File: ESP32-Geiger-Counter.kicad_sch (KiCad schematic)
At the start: 85 parts, among them J1 2s1p Lipo Battery Pack (8.4V-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, J2 USB_C_Receptacle_USB2.0_16P, J5 Conn_01x07, Q1 STN1HNK60, Q3 2N7002, Q4 AO3401A, Q5 MMBT3904, SW1 SW_SPDT, SW2 RESET, SW3 BOOT, U1 BQ25886RGE, U2 AP63203WU, U3 ESP32-S3-WROOM-1, U4 UCC27517DBVR, U5 USBLC6-2SC6, U6 SBM-20 Geiger Mueller Tube

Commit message: layout changes
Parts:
- SW1: footprint Button_Switch_THT:SW_Slide_SPDT_Straight_CK_OS102011MS2Q -> Button_Switch_THT:SW_Slide_SPDT_Angled_CK_OS102011MA1Q
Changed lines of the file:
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@@
 			)
 		)
-		(property "Footprint" "Button_Switch_THT:SW_Slide_SPDT_Straight_CK_OS102011MS2Q"
+		(property "Footprint" "Button_Switch_THT:SW_Slide_SPDT_Angled_CK_OS102011MA1Q"
 			(at 153.67 46.99 0)
 			(hide yes)

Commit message: added test points
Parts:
- added TP_3.3V1: 3.3V, TestPoint:TestPoint_Keystone_5015_Micro_Mini, symbol Connector:TestPoint
- added TP_GND1: GND, TestPoint:TestPoint_Keystone_5015_Micro_Mini, symbol Connector:TestPoint
- added TP_HV_SENSE1: HV_SENSE, TestPoint:TestPoint_Keystone_5015_Micro_Mini, symbol Connector:TestPoint
- added TP_PULSE1: PULSE, TestPoint:TestPoint_Keystone_5015_Micro_Mini, symbol Connector:TestPoint
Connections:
- net +3.3V: now also TP_3.3V1.1
- net GND: now also TP_GND1.1
- net HV_SENSE: now also TP_HV_SENSE1.1
- net PULSE: now also TP_PULSE1.1

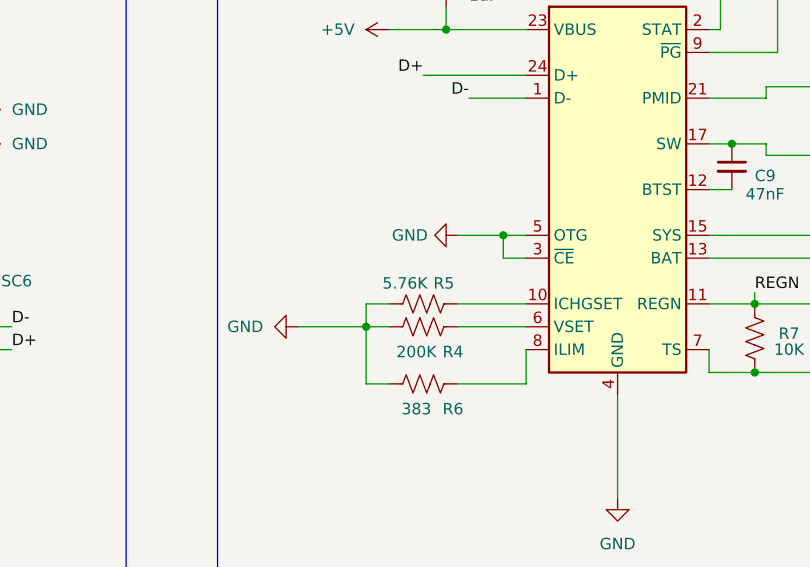
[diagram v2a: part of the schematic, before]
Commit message: pour changes, fixed bad sbm-20 tube footprint
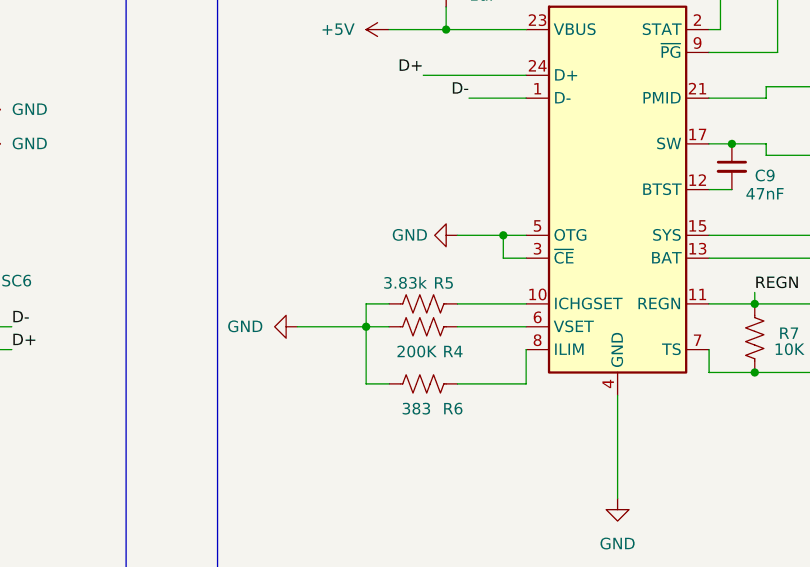
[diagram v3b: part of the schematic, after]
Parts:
- R5: value 5.76K -> 3.83k
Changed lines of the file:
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@@
 			)
 		)
-		(property "Value" "5.76K"
+		(property "Value" "3.83k"
 			(at 138.938 129.794 90)
 			(show_name no)

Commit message: minor passive changes
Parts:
- C26: value 10nF -> 2.2nF
- R19: footprint Resistor_SMD:R_0805_2012Metric -> Resistor_SMD:R_1206_3216Metric
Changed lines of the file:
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@@
 			)
 		)
-		(property "Footprint" "Resistor_SMD:R_0805_2012Metric"
+		(property "Footprint" "Resistor_SMD:R_1206_3216Metric"
 			(at 386.334 203.454 90)
 			(hide yes)
@@
 			)
 		)
-		(property "Value" "10nF"
+		(property "Value" "2.2nF"
 			(at 360.426 248.158 0)
 			(show_name no)
